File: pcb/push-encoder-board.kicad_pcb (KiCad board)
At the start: 2 copper layers, 21 x 30.2 mm, 4 parts

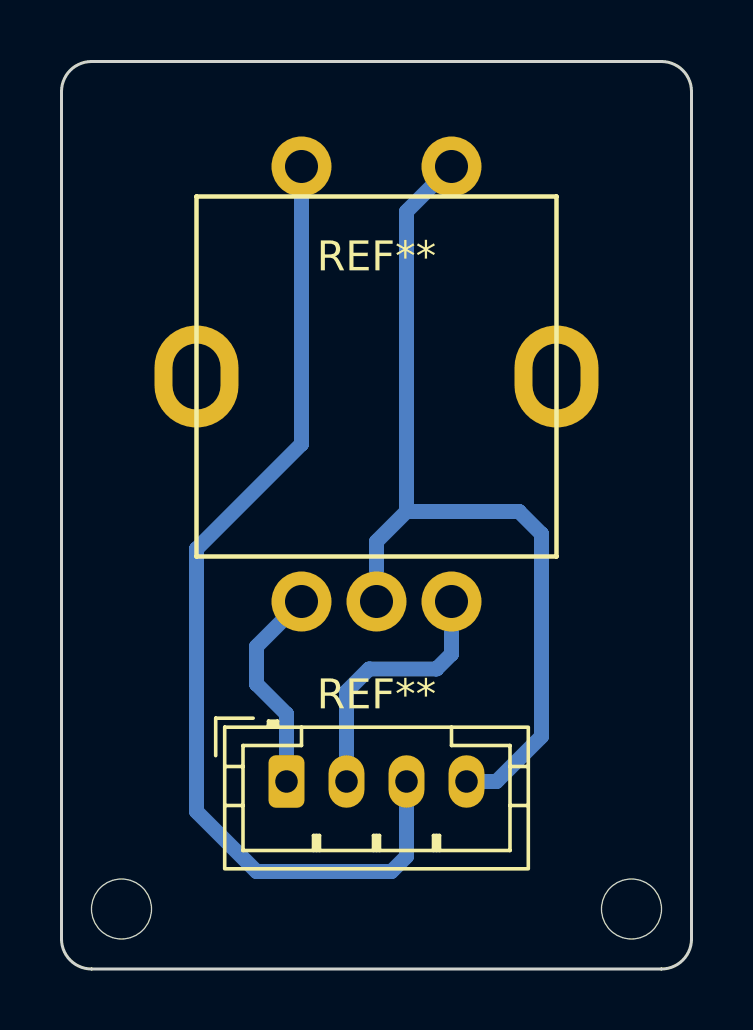
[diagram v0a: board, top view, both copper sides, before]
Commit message: add nc and chenge uf2 for studio
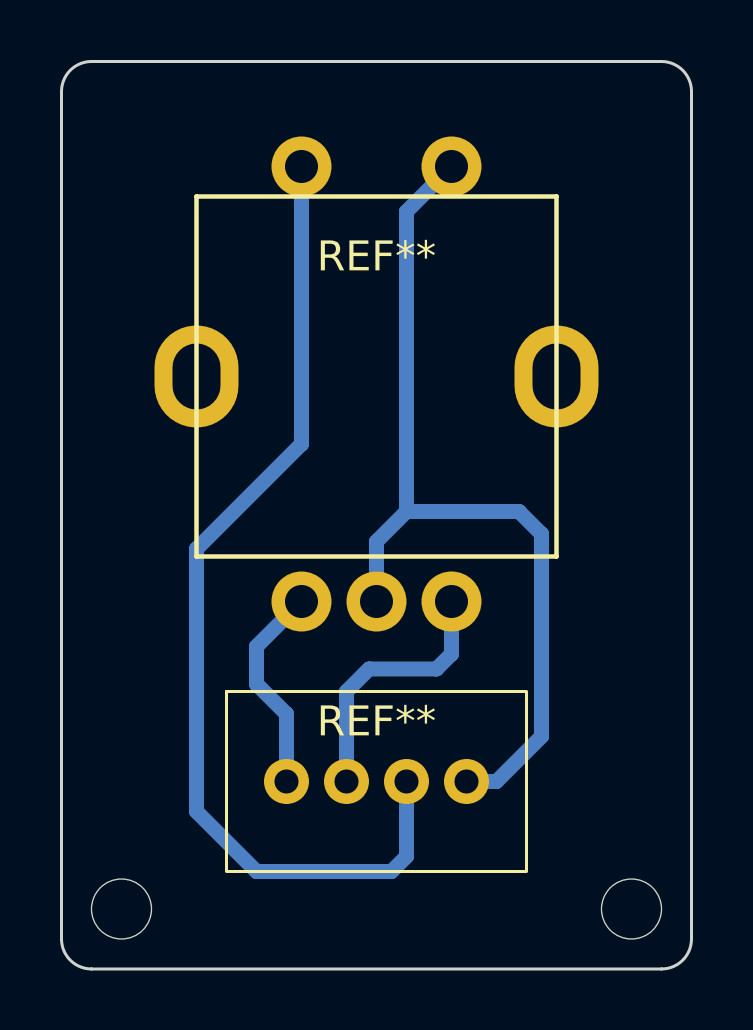
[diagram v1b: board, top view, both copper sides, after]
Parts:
- removed the REF** at (97.0, 88.5)
- added REF**: JST-PH-2-V, Suzuki:JstPh4Vertical, F.Cu at (100.0, 88.5)
